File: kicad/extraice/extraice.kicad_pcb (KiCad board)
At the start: 2 copper layers, 77 x 68.5 mm, 67 parts, among them J1 Conn_01x03, J10 Conn_01x02, J2 Conn_01x03, J3 EncSide, J4 MainSide, J5 Conn_01x05, J6 EncSide, J7 MainSide, J8 Conn_01x02, J9 Conn_01x02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

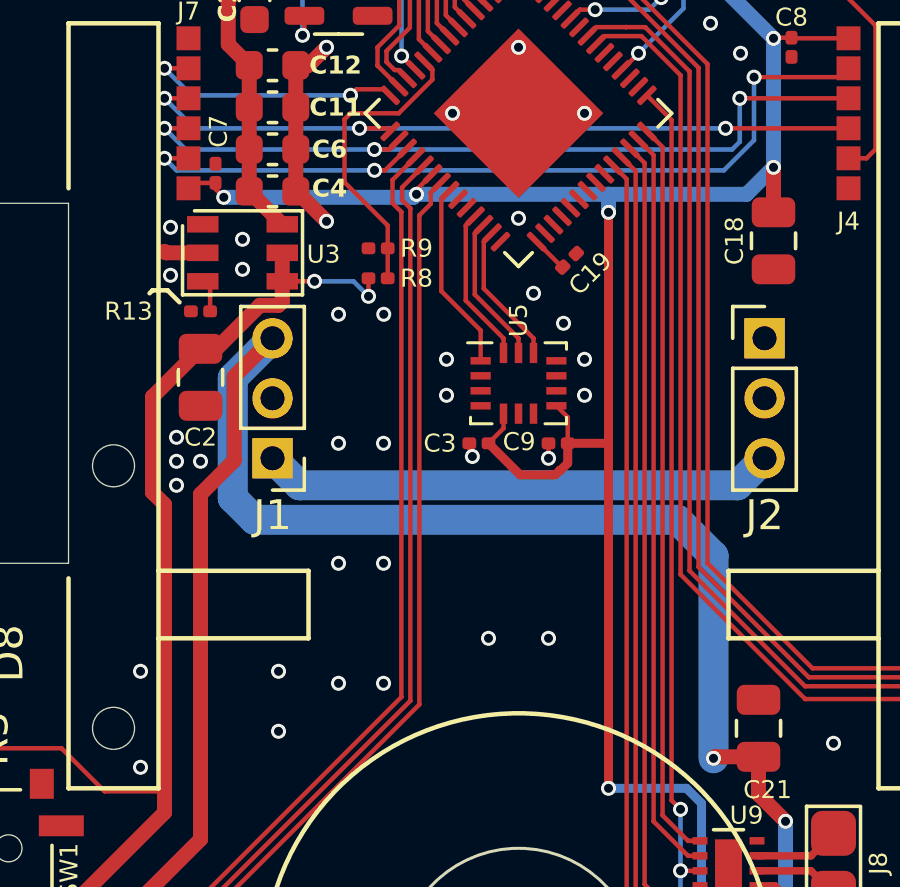
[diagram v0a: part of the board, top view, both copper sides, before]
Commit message: Change some GPIO assignments
Signed-off-by: Kazuki Iida <elkel53930@gmail.com>
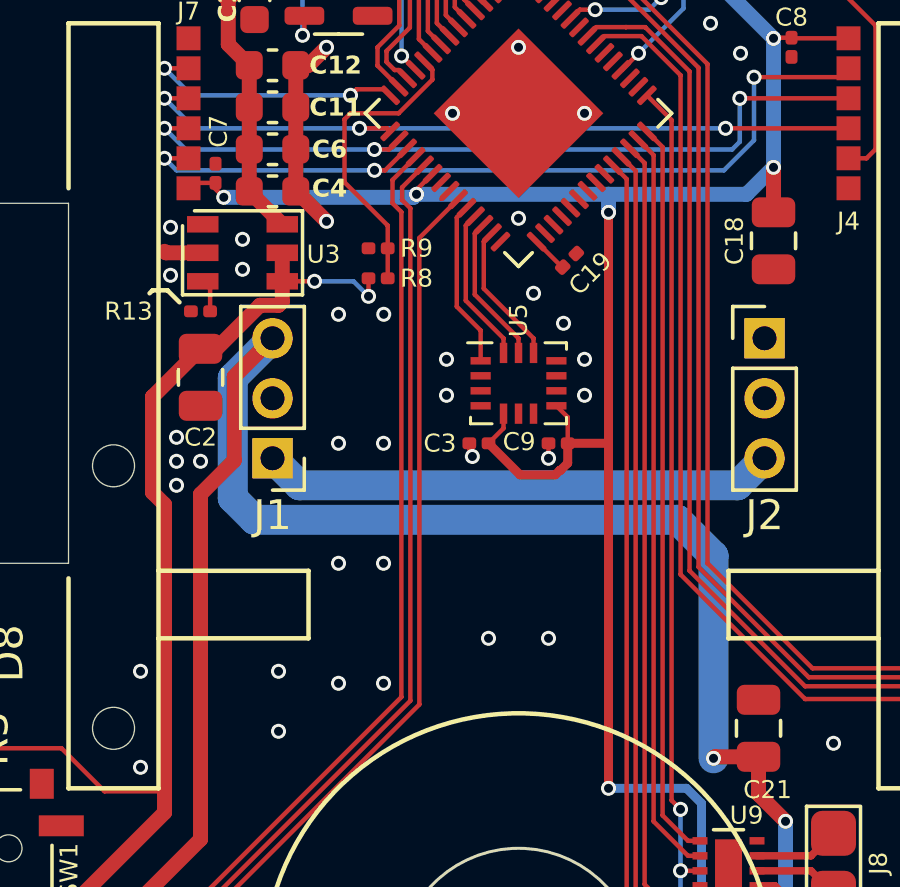
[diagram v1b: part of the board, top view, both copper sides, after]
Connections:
- U7 pad 21: /LED_B -> unconnected-(U7-XTAL_32K_P-Pad21)
- U7 pad 22: /SPI2_MISO -> unconnected-(U7-XTAL_32K_N-Pad22)
- U7 pad 23: unconnected-(U7-GPIO17-Pad23) -> /LED_B
- U7 pad 24: unconnected-(U7-GPIO18-Pad24) -> /SPI2_MISO
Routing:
- net /SPI2_MISO: track 6.33 -> 5.57 mm
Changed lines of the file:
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@@
   (net 3 "+3V0")
   (net 4 "Net-(D8-A)")
-  (net 5 "unconnected-(U7-GPIO17-Pad23)")
+  (net 5 "unconnected-(U7-XTAL_32K_P-Pad21)")
   (net 6 "/SEN_LS")
   (net 7 "/SEN_RF")
   (net 8 "/SEN_RS")
-  (net 9 "unconnected-(U7-GPIO18-Pad24)")
+  (net 9 "unconnected-(U7-XTAL_32K_N-Pad22)")
   (net 10 "/SEN_LF")
   (net 11 "Net-(U3-FB)")
@@
       (net 3 "+3V0") (pinfunction "VDD3P3_RTC") (pintype "power_in"))
     (pad "21" smd roundrect (at -0.2 3.45 315) (size 0.2 0.8) (layers "F.Cu" "F.Paste" "F.Mask") (roundrect_rratio 0.25)
-      (net 73 "/LED_B") (pinfunction "XTAL_32K_P") (pintype "bidirectional"))
+      (net 5 "unconnected-(U7-XTAL_32K_P-Pad21)") (pinfunction "XTAL_32K_P") (pintype "bidirectional+no_connect"))
     (pad "22" smd roundrect (at 0.2 3.45 315) (size 0.2 0.8) (layers "F.Cu" "F.Paste" "F.Mask") (roundrect_rratio 0.25)
-      (net 62 "/SPI2_MISO") (pinfunction "XTAL_32K_N") (pintype "bidirectional"))
+      (net 9 "unconnected-(U7-XTAL_32K_N-Pad22)") (pinfunction "XTAL_32K_N") (pintype "bidirectional+no_connect"))
     (pad "23" smd roundrect (at 0.6 3.45 315) (size 0.2 0.8) (layers "F.Cu" "F.Paste" "F.Mask") (roundrect_rratio 0.25)
-      (net 5 "unconnected-(U7-GPIO17-Pad23)") (pinfunction "GPIO17") (pintype "bidirectional+no_connect"))
+      (net 73 "/LED_B") (pinfunction "GPIO17") (pintype "bidirectional"))
     (pad "24" smd roundrect (at 1 3.45 315) (size 0.2 0.8) (layers "F.Cu" "F.Paste" "F.Mask") (roundrect_rratio 0.25)
-      (net 9 "unconnected-(U7-GPIO18-Pad24)") (pinfunction "GPIO18") (pintype "bidirectional+no_connect"))
+      (net 62 "/SPI2_MISO") (pinfunction "GPIO18") (pintype "bidirectional"))
     (pad "25" smd roundrect (at 1.4 3.45 315) (size 0.2 0.8) (layers "F.Cu" "F.Paste" "F.Mask") (roundrect_rratio 0.25)
       (net 66 "/SPI2_MOSI") (pinfunction "GPIO19") (pintype "bidirectional"))
@@
   (segment (start 148.639376 84.360624) (end 139.133346 84.360624) (width 0.15) (layer "F.Cu") (net 8))
   (segment (start 137.576497 87.727969) (end 137.984746 88.136218) (width 0.15) (layer "F.Cu") (net 8))
+  (segment (start 137.701903 93.58094) (end 137.426903 93.85594) (width 0.15) (layer "F.Cu") (net 9))
   (segment (start 136.977495 88.260338) (end 136.977495 84.750826) (width 0.15) (layer "F.Cu") (net 10))
   (segment (start 137.5 84.228321) (end 137.5 80.704813) (width 0.15) (layer "F.Cu") (net 10))
@@
   (segment (start 137.875998 86.100444) (end 138.76058 85.215862) (width 0.15) (layer "F.Cu") (net 61))
   (segment (start 137.875998 87.461785) (end 137.875998 86.100444) (width 0.15) (layer "F.Cu") (net 61))
-  (segment (start 137.426903 93.85594) (end 137.426903 96.926903) (width 0.15) (layer "F.Cu") (net 62))
-  (segment (start 137.426903 96.926903) (end 138.7375 98.2375) (width 0.15) (layer "F.Cu") (net 62))
+  (segment (start 137.941615 94.472598) (end 137.941615 97.441615) (width 0.15) (layer "F.Cu") (net 62))
   (segment (start 138.7375 98.2375) (end 138.7375 99.25) (width 0.15) (layer "F.Cu") (net 62))
-  (segment (start 137.701903 93.58094) (end 137.426903 93.85594) (width 0.15) (layer "F.Cu") (net 62))
+  (segment (start 138.267588 94.146625) (end 137.941615 94.472598) (width 0.15) (layer "F.Cu") (net 62))
+  (segment (start 137.941615 97.441615) (end 138.7375 98.2375) (width 0.15) (layer "F.Cu") (net 62))
   (segment (start 136.378493 88.144359) (end 136.378493 83.765848) (width 0.15) (layer "F.Cu") (net 63))
   (segment (start 136.012689 89.558274) (end 135.870562 89.558274) (width 0.15) (layer "F.Cu") (net 63))
@@
   (segment (start 128.2 89.5) (end 129.1 90.4) (width 0.15) (layer "B.Cu") (net 72))
   (segment (start 129.1 90.4) (end 134.4 90.4) (width 0.15) (layer "B.Cu") (net 72))
-  (segment (start 136.694501 94.4) (end 136.694501 110.705499) (width 0.15) (layer "F.Cu") (net 73))
-  (segment (start 137.0745 93.642657) (end 137.0745 94.020001) (width 0.15) (layer "F.Cu") (net 73))
   (segment (start 136.694501 110.705499) (end 130 117.4) (width 0.15) (layer "F.Cu") (net 73))
-  (segment (start 137.0745 94.020001) (end 136.694501 94.4) (width 0.15) (layer "F.Cu") (net 73))
   (segment (start 130 117.4) (end 130 119.7125) (width 0.15) (layer "F.Cu") (net 73))
-  (segment (start 137.41906 93.298097) (end 137.0745 93.642657) (width 0.15) (layer "F.Cu") (net 73))
+  (segment (start 137.984746 93.863782) (end 136.694501 95.154027) (width 0.15) (layer "F.Cu") (net 73))
+  (segment (start 136.694501 95.154027) (end 136.694501 110.705499) (width 0.15) (layer "F.Cu") (net 73))
   (segment (start 141.449319 96.126274) (end 140.601041 95.277996) (width 0.15) (layer "F.Cu") (net 75))
   (segment (start 141.473726 96.126274) (end 141.449319 96.126274) (width 0.15) (layer "F.Cu") (net 75))
@@
     (connect_pads (clearance 0.15))
     (min_thickness 0.15) (filled_areas_thickness no)
-    (fill yes (thermal_gap 0.15) (thermal_bridge_width 0.3))
+    (fill (thermal_gap 0.15) (thermal_bridge_width 0.3))
     (polygon
       (pts
